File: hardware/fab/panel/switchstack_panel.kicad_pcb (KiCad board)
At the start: 4 copper layers, 173.4 x 72.4 mm, 220 parts

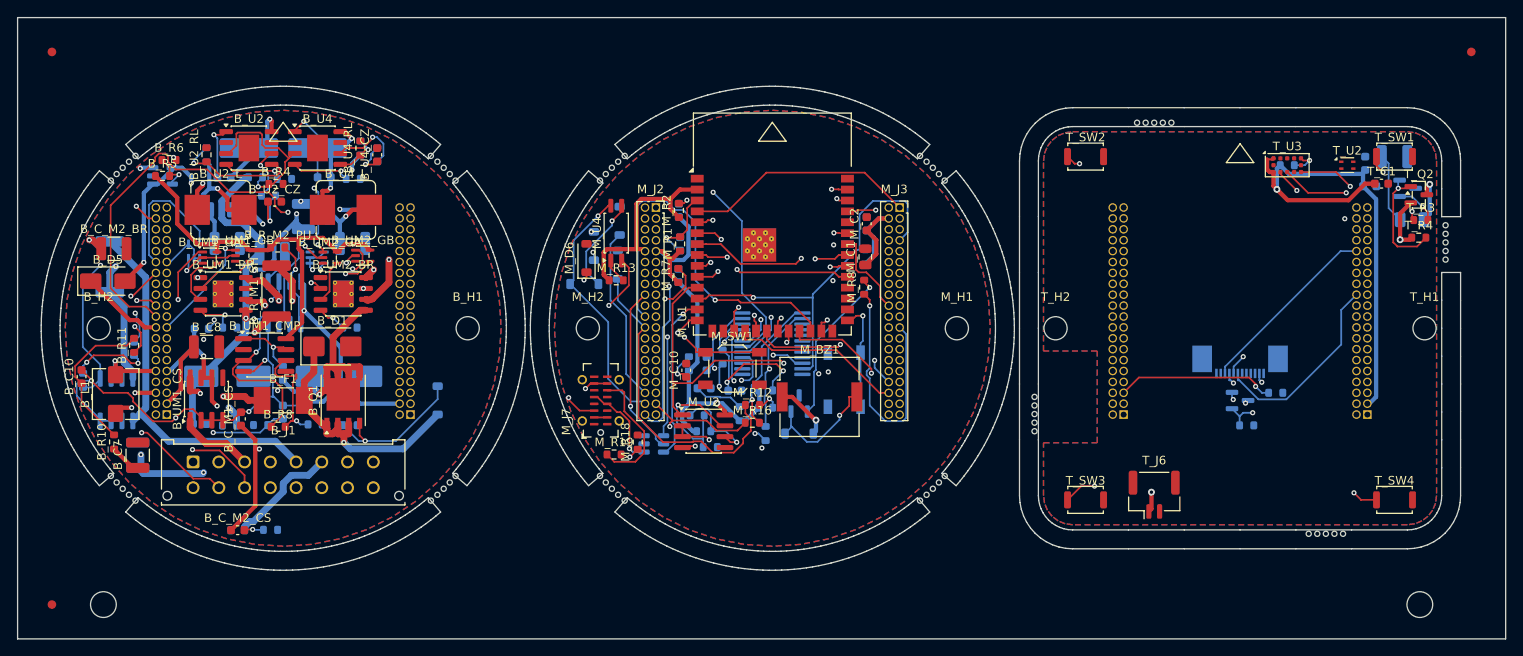
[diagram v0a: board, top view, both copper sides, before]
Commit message: Hauptschalter, Magnetkontakt im Rahmen, verschraubter Stapel - Umbau v0.7
VIER ENTSCHEIDUNGEN VOM 19.08.2026, alle umgesetzt:

1. HAUPTSCHALTER. Bisher stand nach dem Verschrauben von Bottom und Mid
sofort 24 V auf allem - ohne dass das Top-Board steckte. Jetzt laeuft der
Gate-Pulldown des Verpolschutz-FETs als SCHLEIFE durch den Stapel:
Q1-Gate -> R1 -> EN_LOOP (Stapelkontakt B2, war PGND; Pinout v0.7) -> SW5
auf Top -> PGND. Neuer 1-M-Pullup R1B haelt das Gate bei offener Schleife
definiert an der Source. Top-Board fehlt ODER SW5 aus -> Q1 sperrt, nichts
bekommt 24 V. Der Schalter traegt nur den Teilerstrom (~20 uA).
SW5 ist ein Copal CVS-01 (1,5 mm hoch, unter der Scheibe, durch eine
Oeffnung bedienbar). Er sitzt HOCHKANT bei (11,9/-19,4): Das Fenster
zwischen ToF-Courtyard (bis 8,245) und Ecktaster (ab 15,205) ist 6,96 mm
breit, der Schalter waagerecht 7,69 - drei Anlaeufe bei 12,5, 11,0 und 11,9
endeten in DRC-Ueberlappungen, erst das Ausmessen statt Schaetzens der
Courtyards zeigte, dass NUR gedreht Platz ist.

2. MAGNETKONTAKT IN DEN ABDECKRAHMEN, unten mittig - dort haelt auch das
vorhandene DCX-909 (Gewinde OD 8, im Rahmen ist Platz; Messpunkt F14: ist
der Rahmen dort hohl?). Das Magnetlangloch im Top-Board (Zwischenloesung
von einem Tag) ist wieder raus, mit ihm die 6,8-mm-Grenze, an der jedes
Kaufteil scheiterte. Neu: KABELKERBE 5 x 2 unten mittig, J6 dahinter
mittig auf der Rueckseite. Router-Keepout entsprechend getauscht.

3. LOETSCHEIBE hardware/stern_puck/ (OE 16, zweilagig, DRC null Fehler):
verbindet die Steckseite des DCX-909 mit den Litzen des Sterns. Litzen
durch Fesselbohrungen faedeln, umschlagen, loeten - die Zugentlastung ist
die Bohrung, nicht das Zinn. Drei eigene DRC-Runden gebraucht: 2,0er Pads
beruehren sich bei 1,85 Stiftabstand, die Minus-Bruecke lief durch das
Plus-Pad, die Fesselbohrungen brauchten seitliche Lage und OE 16 statt 14.

4. BEFESTIGUNGSKONZEPT v2 (docs/04, 2b): verschraubt statt nur gesteckt.
NEU mechanical/tragring.py 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
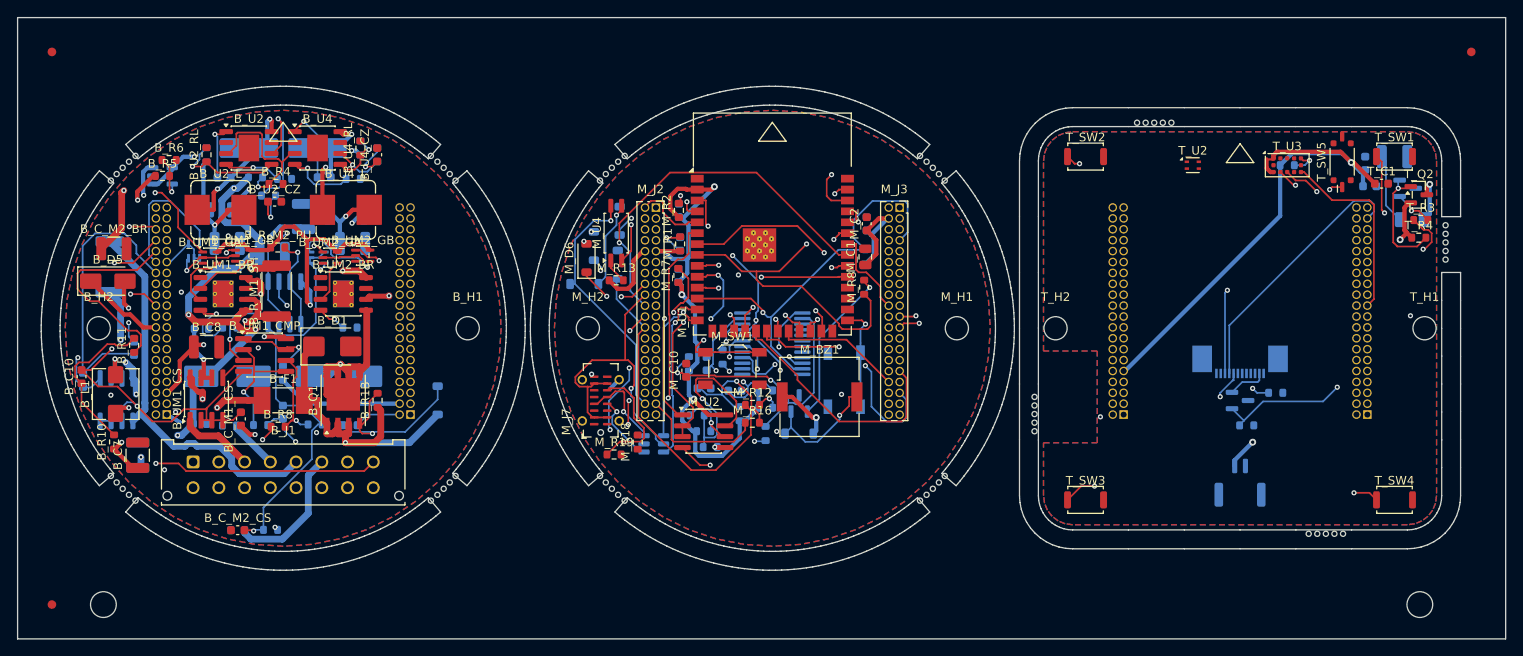
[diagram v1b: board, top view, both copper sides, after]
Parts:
- added B_R1B: 1M, R_0603_1608Metric, F.Cu at (-44.8, 8.40)
- added T_SW5: HAUPT, SW_DIP_SPSTx01_Slide_Copal_CVS-01xB_W5.9mm_P1mm, F.Cu at (67.7, -19.4)
- T_J6: value Stern -> Stern (intern); moved to B.Cu
- moved T_U2 18.0 mm to (50.2, -19.0)
- moved T_J6 10.1 mm to (55.8, 18.0)
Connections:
- B_J3 pad 2: BOT_PGND -> BOT_EN_LOOP
- B_R1 pad 2: BOT_PGND -> BOT_EN_LOOP
- M_J3 pad 2: MID_PGND -> MID_EN_LOOP
- T_J3 pad 2: TOP_PGND -> TOP_EN_LOOP
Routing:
- net BOT_I_SENSE1: track 33.5 -> 66.2 mm, vias 1 -> 2
- net TOP_EN_LOOP: track 0.00 -> 29.1 mm, vias 0 -> 1
- net MID_TRIP_RST: track 52.5 -> 29.1 mm
- net BOT_HOOD_A: track 69.9 -> 46.8 mm
- net TOP_QSPI_CLK: track 22.9 -> 0.00 mm
- net MID_HW_TRIP2: track 21.9 -> 0.00 mm, vias 1 -> 0
- net BOT_M1_ISNS: track 0.00 -> 18.4 mm, vias 0 -> 1
- net MID_USB_CC1: track 15.4 -> 0.00 mm, vias 2 -> 0
- net TOP_STAR_OUT: track 70.1 -> 55.0 mm
- net TOP_DISP_RST: track 43.6 -> 30.6 mm, vias 1 -> 0
- net BOT_3V3_SYS: track 147.8 -> 160.8 mm, vias 5 -> 8
- net MID_RS485_DIR: track 37.0 -> 49.6 mm
- net BOT_M2_INA: track 49.7 -> 37.2 mm, vias 2 -> 1
- net BOT_6V2_STAR_F: track 34.4 -> 45.0 mm, vias 4 -> 2
- net BOT_TRIP_RST: track 13.4 -> 24.0 mm, vias 1 -> 0
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
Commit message: Leistungsvias, Via-Strompruefung, Reset/Boot-Durchgriffe und der Gehaeusebecher
VIER ARBEITEN AUS EINEM ABEND, alle aus Rueckfragen entstanden:

1. VIAS SIND NICHT BELIEBIG STROMTRAGFAEHIG - der Einwand traf: 24V_IN
lief ueber genau EIN 0,6/0,3-Via (~1,2 A) bei 4,1 A Grenzstrom, dazu 14
weitere Engpaesse auf Bottom. Ursache: Die Bottom-Klassen routeten mit dem
Standardvia - ein Erbe der diskreten H-Bruecke, zwischen deren FETs das
0,8er nicht passte; Mid und Top hatten das Leistungsvia laengst. Jetzt:
PWR- und RAIL-Klasse auf Bottom mit 0,8/0,4, Massebruecken dort ebenso
(deren Platzsuche folgt jetzt der Viagroesse - die alte 0,6er-Suche setzte
0,8er-Vias in 0,6er-Luecken, vier Abstandsfehler).

NEU tools/via_check.py: prueft nach jedem Routing jedes Via gegen den
Dauerstrom seines Netzes (4 A je mm Bohrung, 3-mm-Parallelgruppen);
--fix setzt Zwillingsvias. Zwei eigene Fehler auf dem Weg, beide vom
Werkzeug selbst aufgedeckt: KiCad-10-Formabfragen brauchen eine Lage, und
die erste Freiraumpruefung sah nur F/B - ein Via bohrt aber durch ALLE
vier Lagen; 15 Innenlagen-Kurzschluesse, alle rueckstandslos entfernt.
Endstand: 27 Zwillinge gesetzt, 11 dokumentierte Engpaesse als
Handarbeitsliste mit Koordinaten in docs/16.

2. RESET UND BOOT WAREN UNERREICHBAR - SW1 sass mitten unter dem
Top-Board, SW2 zeigte zur Rueckseite. Beide jetzt auf Mids Vorderseite bei
(+-8/18,6), darueber zwei OE-3,2-Durchgriffe H3/H4 im Top-Board: Scheibe
ab, Stift durch, druecken. Im Betrieb verdeckt die Scheibe die Loecher.

3. DER GEHAEUSEBECHER (mechanical/gehaeuse.py): kapselt Bottom und Mid,
Rueckwand mit Tunnelfenster fuer die Feldstecker-Leiste - sie bleibt als
einziges von hinten zugaenglich. Verbindung zum Tragring per BAJONETT:
drei Zapfen an 12/3/9 Uhr, ~7 Grad Drehung, tangential auskragende
Koepfe - radiale Rasthaken scheiterten dreifach (Adapter auf den
Diagonalen, Dosenwand aussen, Adapterbasis innen; frei ist nur ein
2,2-mm-Band auf den Achsen). Wand an den Schraubdomen gefenste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
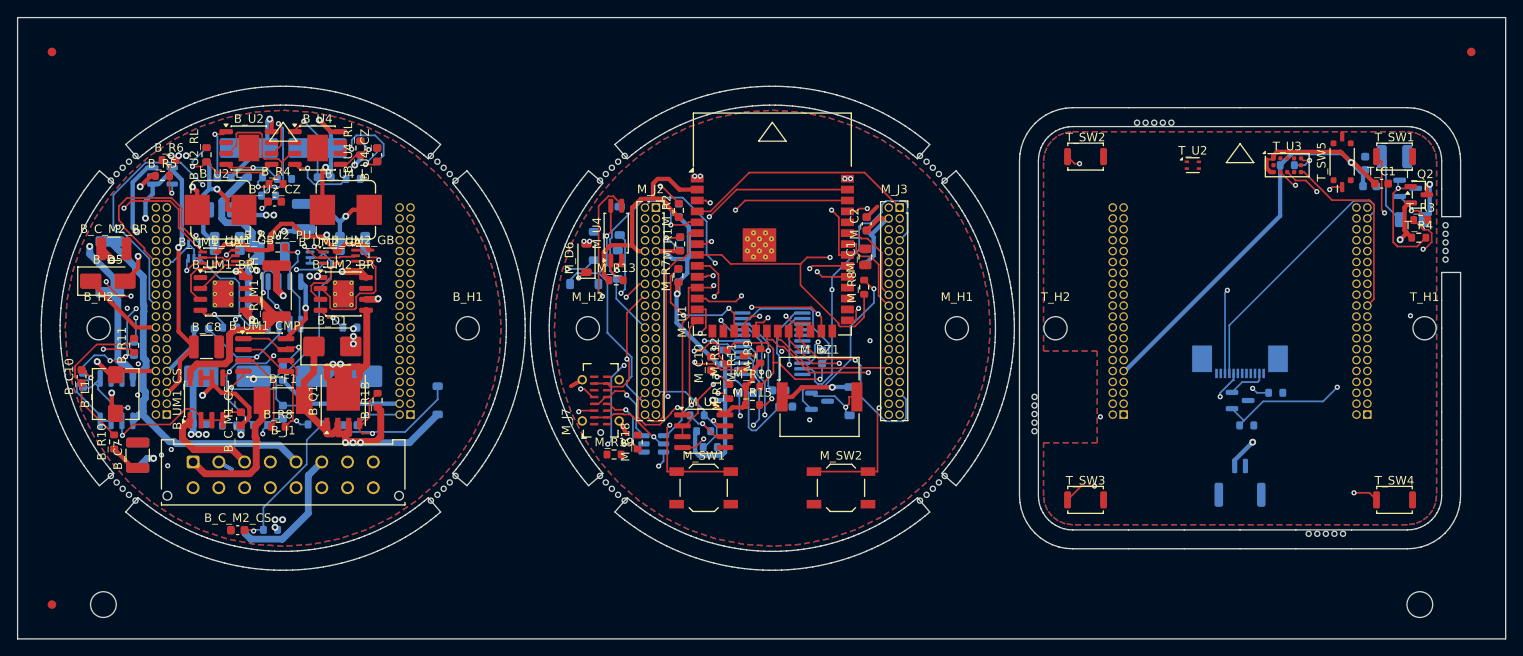
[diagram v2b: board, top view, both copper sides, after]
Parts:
- M_R10, M_R11, M_R15, M_R17, M_R9, M_SW2: moved to F.Cu
- M_R16: moved to B.Cu
- moved M_SW1 14.3 mm to (-6.75, 18.6)
- moved M_C8 13.5 mm to (7.05, 3.35)
- moved M_SW2 12.6 mm to (9.25, 18.6), turned to 0 degrees
- moved M_C9 9.75 mm to (2.81, 9.14)
- moved M_R15 8.82 mm to (-1.07, 8.93), turned to 0 degrees
- moved M_D1 6.98 mm to (10.2, 8.50), turned to 90 degrees
- moved M_R14 6.90 mm to (-4.55, 3.35)
- moved M_R17 6.47 mm to (-3.77, 7.37)
- moved M_R12 6.32 mm to (-4.03, 3.35), turned to 90 degrees
- moved M_C7 5.15 mm to (2.03, 7.24)
- moved M_R9 4.08 mm to (-0.16, 3.21), turned to 90 degrees
- moved M_R16 3.52 mm to (-1.77, 7.56)
- moved M_C10 3.00 mm to (-5.88, 4.12)
- moved M_R10 2.88 mm to (-1.03, 6.80)
- moved M_R11 2.56 mm to (-2.08, 4.02)
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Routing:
- net BOT_I_SENSE1: track 66.2 -> 36.5 mm, vias 2 -> 3
- net BOT_M2_ISNS: track 66.2 -> 40.2 mm
- net BOT_6V2_STAR_F: track 45.0 -> 23.8 mm, vias 2 -> 1
- net MID_ESP_BOOT: track 43.1 -> 62.3 mm
- net BOT_24V_PROT: track 135.7 -> 116.7 mm, vias 7 -> 9
- net MID_SAB1_IN: track 41.6 -> 59.3 mm, vias 1 -> 2
- net MID_EXP_P7: track 19.3 -> 35.2 mm, vias 2 -> 1
- net BOT_I_SENSE2: track 33.4 -> 18.7 mm, vias 0 -> 3
- net BOT_V_TRIP_HI: track 36.9 -> 22.5 mm, vias 2 -> 1
- net MID_PGND: track 6.00 -> 20.0 mm, vias 4 -> 7
- net MID_RS485_B: track 28.1 -> 14.1 mm
- net MID_USB_CC2: track 14.0 -> 0.00 mm
- net MID_M2_INB: track 54.9 -> 41.0 mm, vias 3 -> 1
- net MID_TRIP_RST: track 29.1 -> 42.9 mm, vias 1 -> 3
- net BOT_M2_GB: track 0.00 -> 13.5 mm
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
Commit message: Bestellfaehigkeit Punkt fuer Punkt - und das Flip-Flop war unbestueckbar
Die Frage "was ist entscheidend fuer Fertigung und Bestueckung?" wurde als
Sieben-Punkte-Liste beantwortet und abgearbeitet:

1. NETZE: Zweiter Freerouting-Pass ueber alle drei Boards - die neue
Erkenntnis (Altbahnen gelten als Vorverdrahtung) als Werkzeug genutzt.
Mid faellt auf 3 offene Signale. Top ist geometrisch festgefahren (9),
Bottom nach Neuerzeugung bei seinen Restnetzen - alles dokumentierte
Handarbeit in docs/16. gen_fab bleibt bis dahin zu Recht verriegelt.

2. KUPFER: Alle drei Boards null Fehler. Drei Nacharbeiten auf dem Weg:
ein Brueckenvia 0,33 mm vor der Bottom-Kante nach innen gerueckt, das
RELAY_CTL-Segment an der USB-Bohrung erneut entfernt (Freerouting legt es
in dieselbe Luecke - ein Keepout scheidet aus, weil die USB-Pads nur
1,0 mm neben den Loechern liegen; bleibt Handarbeit), und die
LCSC-Felder unsichtbar gestellt, die als sieben ungespiegelte C-Nummern
im Bestueckungsdruck der Rueckseite auftauchten.

3. LCSC: 13 Nummern verifiziert (jede von einer LCSC-Produktseite,
nichts geraten) und doppelt verdrahtet - in den Schaltplan-Generatoren
fuer kuenftige Neuerzeugungen, per neuem tools/lcsc_nachtragen.py auf
den fertig gerouteten Boards. Fehlend: 262 statt 302. Ehrlich offen:
TLV3702 (LCSC fuehrt nur die TLC-Variante, die am Gleichtaktbereich
scheitert), VL53L1X, Micro-Fit 43045-1612 (THT, zur Not von Hand).

DER WICHTIGSTE FUND STECKTE IM LCSC-ABGLEICH: Das Trip-Latch 74AUP1G74
stand im 5-Pin-SOT-353 - ein D-Flip-Flop hat ACHT Pins, 6/7/8 hingen in
der Luft. Jedes gefertigte Bottom waere Schrott gewesen. Jetzt VSSOP-8
(SN74AUP1G74DCUR, C140267), Bottom komplett neu erzeugt und geroutet -
974 Segmente, 121 Vias, mit SENSE-Abstandsklasse (300 um) fuer
M1_ISNS/M2_ISNS gegen die Trip-Schwellen.

4. NUTZEN: kupferfehlerfrei; die zwoelf verbleibenden DRC-Meldungen sind
EINE Sache (Mausbiss-Bohrungen des 12-Uhr-Stegs in der grosszuegigen
ESP32-Sperrflaeche - kein Kupfer, en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
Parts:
- removed the B_UM1_FF at (-66.1, -8.99)
- removed the B_UM2_FF at (-51.8, -8.23)
- added B_UM1_FF: 74AUP1G74, VSSOP-8_2.3x2mm_P0.5mm, F.Cu at (-62.5, -8.50)
- added B_UM2_FF: 74AUP1G74, VSSOP-8_2.3x2mm_P0.5mm, F.Cu at (-57.0, -10.8)
- added T_H3: MountingHole_3.2mm_M3, MountingHole_3.2mm_M3, F.Cu at (47.8, 18.6)
- added T_H4: MountingHole_3.2mm_M3, MountingHole_3.2mm_M3, F.Cu at (63.8, 18.6)
- B_C10, B_R_M2_PU, B_UM1_GA, B_UM1_GB: moved to B.Cu
- B_R12: moved to F.Cu
- T_J6: footprint JST_GH_BM02B-GHS-TBT_1x02-1MP_P1.25mm_Vertical -> JST_GH_SM02B-GHS-TB_1x02-1MP_P1.25mm_Horizontal
- moved B_R10 32.4 mm to (-54.6, -11.6)
- moved B_R12 20.9 mm to (-75.5, 13.2), turned to 90 degrees
- moved B_C10 19.7 mm to (-73.1, -13.1)
- moved T_R_BLG 15.9 mm to (55.0, -4.52)
- moved B_R11 15.1 mm to (-73.1, -13.1)
- moved T_Q_BL 10.0 mm to (55.8, -1.62)
- moved B_UM1_GB 4.56 mm to (-57.6, -12.0)
- moved B_R_M2_PU 3.99 mm to (-52.6, -8.15)
- moved T_R_BL 3.47 mm to (56.5, 8.32)
- moved B_UM1_GA 2.18 mm to (-66.4, -8.76), turned to 90 degrees
- moved T_J5 1.04 mm to (55.8, 2.88), turned to 180 degrees
- moved T_J6 0.45 mm to (55.8, 18.4), turned to 180 degrees
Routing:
- net BOT_M1_A: track 43.4 -> 97.3 mm
- net BOT_M1_TRIP: track 10.1 -> 55.2 mm, vias 1 -> 3
- net BOT_3V3_SYS: track 160.4 -> 198.8 mm, vias 5 -> 7
- net BOT_V_TRIP_HI: track 22.5 -> 52.8 mm, vias 1 -> 3
- net TOP_3V3_SYS: track 92.8 -> 66.4 mm
- net BOT_M1_GB: track 7.07 -> 30.0 mm, vias 0 -> 2
- net BOT_TRIP_RST: track 22.7 -> 4.38 mm, vias 3 -> 0
- net BOT_M1_INA: track 31.0 -> 49.0 mm, vias 1 -> 4
- net TOP_QSPI_CLK: track 0.00 -> 18.0 mm, vias 0 -> 1
- net BOT_6V2_STAR_F: track 23.8 -> 41.2 mm, vias 1 -> 2
- net TOP_5V_SYS: track 21.1 -> 3.81 mm, vias 1 -> 0
- net BOT_SAB1_IN: track 35.1 -> 50.7 mm, vias 0 -> 1
- net BOT_AGND: track 151.6 -> 137.6 mm, vias 6 -> 3
- net BOT_M2_INA: track 40.6 -> 53.1 mm
- net TOP_DISP_BL: track 35.8 -> 23.4 mm, vias 1 -> 0
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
